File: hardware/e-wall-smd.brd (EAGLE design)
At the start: 50.8 x 48.3 mm, 66 parts, among them IC1 74HCT595D, IC2 74HCT595D, IC3 74HCT595D, IC4 74HCT595D, Q1 2N7002P, Q10 2N7002P, Q11 2N7002P, Q12 2N7002P, Q13 2N7002P, Q14 2N7002P, Q15 2N7002P, Q16 2N7002P, Q17 2N7002P, Q18 2N7002P, Q19 2N7002P, Q2 2N7002P, Q20 2N7002P, Q21 2N7002P, Q22 2N7002P, Q23 2N7002P, Q24 2N7002P, Q25 IRF8313P, Q26 IRF8313P, Q27 IRF8313P, Q28 IRF8313P, Q29 2N7002P, Q3 2N7002P, Q30 2N7002P, Q31 BSS84, Q4 2N7002P, Q5 2N7002P, Q6 2N7002P, Q7 2N7002P, Q8 2N7002P, Q9 2N7002P

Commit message: Transistortypen festgelegt
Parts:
- Q1, Q10, Q11, Q12, Q13, Q14, Q15, Q16, Q17, Q18, Q19, Q2, Q20, Q21, Q22, Q23, Q24, Q29, Q3, Q30, Q4, Q5, Q6, Q7, Q8, Q9: value 2N7002P -> SI2302CDS
- Q25, Q26, Q27, Q28: value IRF8313P -> SI4214DDY
- Q31: value BSS84 -> SI2347DS
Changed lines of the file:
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@@
 <element name="U$2" library="ultrasonic" package="HC-SR04" value="HC-SR04" x="25.4" y="2.54"/>
 <element name="U$1" library="msp430launchpad" package="MSP430LAUNCHPAD_BASIC" value="MSP430G2 Launchpad" x="25.4" y="13.97"/>
-<element name="Q1" library="transistor-small-signal" package="SOT23" value="2N7002P" x="8.89" y="26.67" rot="R90"/>
-<element name="Q2" library="transistor-small-signal" package="SOT23" value="2N7002P" x="8.89" y="27.94" rot="MR270"/>
-<element name="Q3" library="transistor-small-signal" package="SOT23" value="2N7002P" x="8.89" y="30.48" rot="R90"/>
-<element name="Q4" library="transistor-small-signal" package="SOT23" value="2N7002P" x="8.89" y="31.75" rot="MR270"/>
-<element name="Q5" library="transistor-small-signal" package="SOT23" value="2N7002P" x="8.89" y="35.56" rot="R90"/>
-<element name="Q6" library="transistor-small-signal" package="SOT23" value="2N7002P" x="8.89" y="36.83" rot="MR270"/>
-<element name="Q7" library="transistor-small-signal" package="SOT23" value="2N7002P" x="8.89" y="39.37" rot="R90"/>
-<element name="Q8" library="transistor-small-signal" package="SOT23" value="2N7002P" x="8.89" y="40.64" rot="MR270"/>
-<element name="Q9" library="transistor-small-signal" package="SOT23" value="2N7002P" x="31.75" y="39.37"/>
-<element name="Q10" library="transistor-small-signal" package="SOT23" value="2N7002P" x="30.48" y="39.37" rot="MR0"/>
-<element name="Q11" library="transistor-small-signal" package="SOT23" value="2N7002P" x="27.94" y="39.37"/>
-<element name="Q12" library="transistor-small-signal" package="SOT23" value="2N7002P" x="26.67" y="39.37" rot="MR0"/>
-<element name="Q13" library="transistor-small-signal" package="SOT23" value="2N7002P" x="24.13" y="39.37"/>
-<element name="Q14" library="transistor-small-signal" package="SOT23" value="2N7002P" x="22.86" y="39.37" rot="MR0"/>
-<element name="Q15" library="transistor-small-signal" package="SOT23" value="2N7002P" x="20.32" y="39.37"/>
-<element name="Q16" library="transistor-small-signal" package="SOT23" value="2N7002P" x="19.05" y="39.37" rot="MR0"/>
-<element name="Q17" library="transistor-small-signal" package="SOT23" value="2N7002P" x="41.91" y="40.64" rot="R270"/>
-<element name="Q18" library="transistor-small-signal" package="SOT23" value="2N7002P" x="41.91" y="39.37" rot="MR90"/>
-<element name="Q19" library="transistor-small-signal" package="SOT23" value="2N7002P" x="41.91" y="36.83" rot="R270"/>
-<element name="Q20" library="transistor-small-signal" package="SOT23" value="2N7002P" x="41.91" y="35.56" rot="MR90"/>
-<element name="Q21" library="transistor-small-signal" package="SOT23" value="2N7002P" x="41.91" y="33.02" rot="R270"/>
-<element name="Q22" library="transistor-small-signal" package="SOT23" value="2N7002P" x="41.91" y="31.75" rot="MR90"/>
-<element name="Q23" library="transistor-small-signal" package="SOT23" value="2N7002P" x="41.91" y="29.21" rot="R270"/>
-<element name="Q24" library="transistor-small-signal" package="SOT23" value="2N7002P" x="41.91" y="27.94" rot="MR90"/>
+<element name="Q1" library="transistor-small-signal" package="SOT23" value="SI2302CDS" x="8.89" y="26.67" rot="R90"/>
+<element name="Q2" library="transistor-small-signal" package="SOT23" value="SI2302CDS" x="8.89" y="27.94" rot="MR270"/>
+<element name="Q3" library="transistor-small-signal" package="SOT23" value="SI2302CDS" x="8.89" y="30.48" rot="R90"/>
+<element name="Q4" library="transistor-small-signal" package="SOT23" value="SI2302CDS" x="8.89" y="31.75" rot="MR270"/>
+<element name="Q5" library="transistor-small-signal" package="SOT23" value="SI2302CDS" x="8.89" y="35.56" rot="R90"/>
+<element name="Q6" library="transistor-small-signal" package="SOT23" value="SI2302CDS" x="8.89" y="36.83" rot="MR270"/>
+<element name="Q7" library="transistor-small-signal" package="SOT23" value="SI2302CDS" x="8.89" y="39.37" rot="R90"/>
+<element name="Q8" library="transistor-small-signal" package="SOT23" value="SI2302CDS" x="8.89" y="40.64" rot="MR270"/>
+<element name="Q9" library="transistor-small-signal" package="SOT23" value="SI2302CDS" x="31.75" y="39.37"/>
+<element name="Q10" library="transistor-small-signal" package="SOT23" value="SI2302CDS" x="30.48" y="39.37" rot="MR0"/>
+<element name="Q11" library="transistor-small-signal" package="SOT23" value="SI2302CDS" x="27.94" y="39.37"/>
+<element name="Q12" library="transistor-small-signal" package="SOT23" value="SI2302CDS" x="26.67" y="39.37" rot="MR0"/>
+<element name="Q13" library="transistor-small-signal" package="SOT23" value="SI2302CDS" x="24.13" y="39.37"/>
+<element name="Q14" library="transistor-small-signal" package="SOT23" value="SI2302CDS" x="22.86" y="39.37" rot="MR0"/>
+<element name="Q15" library="transistor-small-signal" package="SOT23" value="SI2302CDS" x="20.32" y="39.37"/>
+<element name="Q16" library="transistor-small-signal" package="SOT23" value="SI2302CDS" x="19.05" y="39.37" rot="MR0"/>
+<element name="Q17" library="transistor-small-signal" package="SOT23" value="SI2302CDS" x="41.91" y="40.64" rot="R270"/>
+<element name="Q18" library="transistor-small-signal" package="SOT23" value="SI2302CDS" x="41.91" y="39.37" rot="MR90"/>
+<element name="Q19" library="transistor-small-signal" package="SOT23" value="SI2302CDS" x="41.91" y="36.83" rot="R270"/>
+<element name="Q20" library="transistor-small-signal" package="SOT23" value="SI2302CDS" x="41.91" y="35.56" rot="MR90"/>
+<element name="Q21" library="transistor-small-signal" package="SOT23" value="SI2302CDS" x="41.91" y="33.02" rot="R270"/>
+<element name="Q22" library="transistor-small-signal" package="SOT23" value="SI2302CDS" x="41.91" y="31.75" rot="MR90"/>
+<element name="Q23" library="transistor-small-signal" package="SOT23" value="SI2302CDS" x="41.91" y="29.21" rot="R270"/>
+<element name="Q24" library="transistor-small-signal" package="SOT23" value="SI2302CDS" x="41.91" y="27.94" rot="MR90"/>
 <element name="D1" library="diode" package="SOT23" value="BAS40-05" x="3.81" y="29.21" rot="MR270"/>
 <element name="D2" library="diode" package="SOT23" value="BAS40-05" x="3.81" y="34.29" rot="MR270"/>
@@
 <element name="D12" library="diode" package="SOT23" value="BAS40-05" x="46.99" y="29.21" rot="MR90"/>
 <element name="IC4" library="74xx-eu" package="SO16" value="74HCT595D" x="25.4" y="15.24"/>
-<element name="Q25" library="transistor-power" package="SO-08" value="IRF8313P" x="19.05" y="16.51" rot="MR270"/>
-<element name="Q26" library="transistor-power" package="SO-08" value="IRF8313P" x="19.05" y="10.16" rot="MR270"/>
-<element name="Q27" library="transistor-power" package="SO-08" value="IRF8313P" x="31.75" y="10.16" rot="MR90"/>
-<element name="Q28" library="transistor-power" package="SO-08" value="IRF8313P" x="31.75" y="16.51" rot="MR90"/>
+<element name="Q25" library="transistor-power" package="SO-08" value="SI4214DDY" x="19.05" y="16.51" rot="MR270"/>
+<element name="Q26" library="transistor-power" package="SO-08" value="SI4214DDY" x="19.05" y="10.16" rot="MR270"/>
+<element name="Q27" library="transistor-power" package="SO-08" value="SI4214DDY" x="31.75" y="10.16" rot="MR90"/>
+<element name="Q28" library="transistor-power" package="SO-08" value="SI4214DDY" x="31.75" y="16.51" rot="MR90"/>
 <element name="SV4" library="con-lstb" package="MA04-2" value="" x="11.43" y="15.24" rot="MR90">
 <attribute name="OC_NEWARK" value="unknown" x="11.43" y="15.24" size="1.778" layer="28" rot="MR90" display="off"/>
@@
 <attribute name="TP_SIGNAL_NAME" value="" x="35.56" y="39.37" size="1.778" layer="27" display="off"/>
 </element>
-<element name="Q29" library="transistor-small-signal" package="SOT23" value="2N7002P" x="38.1" y="2.54" rot="MR90"/>
-<element name="Q30" library="transistor-small-signal" package="SOT23" value="2N7002P" x="12.7" y="3.81" rot="R270"/>
-<element name="Q31" library="transistor-small-signal" package="SOT23" value="BSS84" x="22.86" y="5.08" rot="R270"/>
+<element name="Q29" library="transistor-small-signal" package="SOT23" value="SI2302CDS" x="38.1" y="2.54" rot="MR90"/>
+<element name="Q30" library="transistor-small-signal" package="SOT23" value="SI2302CDS" x="12.7" y="3.81" rot="R270"/>
+<element name="Q31" library="transistor-small-signal" package="SOT23" value="SI2347DS" x="22.86" y="5.08" rot="R270"/>
 </elements>
 <signals>

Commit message: kleine Anpassungen im Schema, erc bereinigt
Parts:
- SV1, SV2, SV3: value (none) -> 8x2
- SV4, SV5: value (none) -> 4x2
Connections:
- net +5V: now also U$2.1; no longer U$2.P$1
- net ECHO: now also U$2.3; no longer U$2.P$3
- net GND: now also U$2.4; no longer U$2.P$4
- net TRIGGER: now also U$2.2; no longer U$2.P$2
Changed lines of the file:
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@@
 <element name="R6" library="resistor" package="R1206" value="4.7k" x="27.94" y="5.08" rot="R180"/>
 <element name="R7" library="resistor" package="R1206" value="100k" x="6.35" y="3.81" rot="MR0"/>
-<element name="SV1" library="con-lsta" package="FE08-2" value="" x="3.81" y="36.83" rot="MR270">
+<element name="SV1" library="con-lsta" package="FE08-2" value="8x2" x="3.81" y="36.83" rot="MR270">
 <attribute name="OC_NEWARK" value="unknown" x="66.04" y="-12.7" size="1.778" layer="28" rot="MR270" display="off"/>
 <attribute name="MPN" value="" x="66.04" y="-12.7" size="1.778" layer="28" rot="MR270" display="off"/>
@@
 <attribute name="OC_FARNELL" value="unknown" x="66.04" y="-12.7" size="1.778" layer="28" rot="MR270" display="off"/>
 </element>
-<element name="SV2" library="con-lsta" package="FE08-2" value="" x="25.4" y="44.45">
+<element name="SV2" library="con-lsta" package="FE08-2" value="8x2" x="25.4" y="44.45">
 <attribute name="OC_NEWARK" value="unknown" x="96.52" y="-17.78" size="1.778" layer="27" display="off"/>
 <attribute name="MPN" value="" x="96.52" y="-17.78" size="1.778" layer="27" display="off"/>
@@
 <attribute name="OC_FARNELL" value="unknown" x="96.52" y="-17.78" size="1.778" layer="27" display="off"/>
 </element>
-<element name="SV3" library="con-lsta" package="FE08-2" value="" x="46.99" y="36.83" rot="MR90">
+<element name="SV3" library="con-lsta" package="FE08-2" value="8x2" x="46.99" y="36.83" rot="MR90">
 <attribute name="OC_NEWARK" value="unknown" x="-27.94" y="60.96" size="1.778" layer="28" rot="MR90" display="off"/>
 <attribute name="MPN" value="" x="-27.94" y="60.96" size="1.778" layer="28" rot="MR90" display="off"/>
@@
 <element name="Q27" library="transistor-power" package="SO-08" value="SI4214DDY" x="31.75" y="10.16" rot="MR90"/>
 <element name="Q28" library="transistor-power" package="SO-08" value="SI4214DDY" x="31.75" y="16.51" rot="MR90"/>
-<element name="SV4" library="con-lstb" package="MA04-2" value="" x="11.43" y="15.24" rot="MR90">
+<element name="SV4" library="con-lstb" package="MA04-2" value="4x2" x="11.43" y="15.24" rot="MR90">
 <attribute name="OC_NEWARK" value="unknown" x="11.43" y="15.24" size="1.778" layer="28" rot="MR90" display="off"/>
 <attribute name="MPN" value="" x="11.43" y="15.24" size="1.778" layer="28" rot="MR90" display="off"/>
@@
 <attribute name="OC_FARNELL" value="unknown" x="11.43" y="15.24" size="1.778" layer="28" rot="MR90" display="off"/>
 </element>
-<element name="SV5" library="con-lstb" package="MA04-2" value="" x="39.37" y="15.24" rot="MR270">
+<element name="SV5" library="con-lstb" package="MA04-2" value="4x2" x="39.37" y="15.24" rot="MR270">
 <attribute name="OC_NEWARK" value="unknown" x="39.37" y="15.24" size="1.778" layer="28" rot="MR270" display="off"/>
 <attribute name="MPN" value="" x="39.37" y="15.24" size="1.778" layer="28" rot="MR270" display="off"/>
@@
 <signal name="ECHO">
 <contactref element="R1" pad="2"/>
-<contactref element="U$2" pad="P$3"/>
+<contactref element="U$2" pad="3"/>
 <wire x1="7.772" y1="2.54" x2="8.636" y2="2.54" width="0.4064" layer="1"/>
 <wire x1="8.636" y1="2.54" x2="10.16" y2="1.016" width="0.4064" layer="1"/>
@@
 <signal name="TRIGGER">
 <contactref element="R6" pad="2"/>
-<contactref element="U$2" pad="P$2"/>
+<contactref element="U$2" pad="2"/>
 <contactref element="Q31" pad="3"/>
 <wire x1="24.13" y1="2.54" x2="24.13" y2="4.91" width="0.4064" layer="1"/>
@@
 <signal name="+5V" class="1">
 <contactref element="R4" pad="2"/>
-<contactref element="U$2" pad="P$1"/>
+<contactref element="U$2" pad="1"/>
 <contactref element="IC1" pad="10"/>
 <contactref element="IC2" pad="10"/>
@@
 <contactref element="R6" pad="1"/>
 <contactref element="R9" pad="1"/>
-<contactref element="U$2" pad="P$4"/>
+<contactref element="U$2" pad="4"/>
 <contactref element="U$1" pad="20"/>
 <contactref element="Q6" pad="2"/>

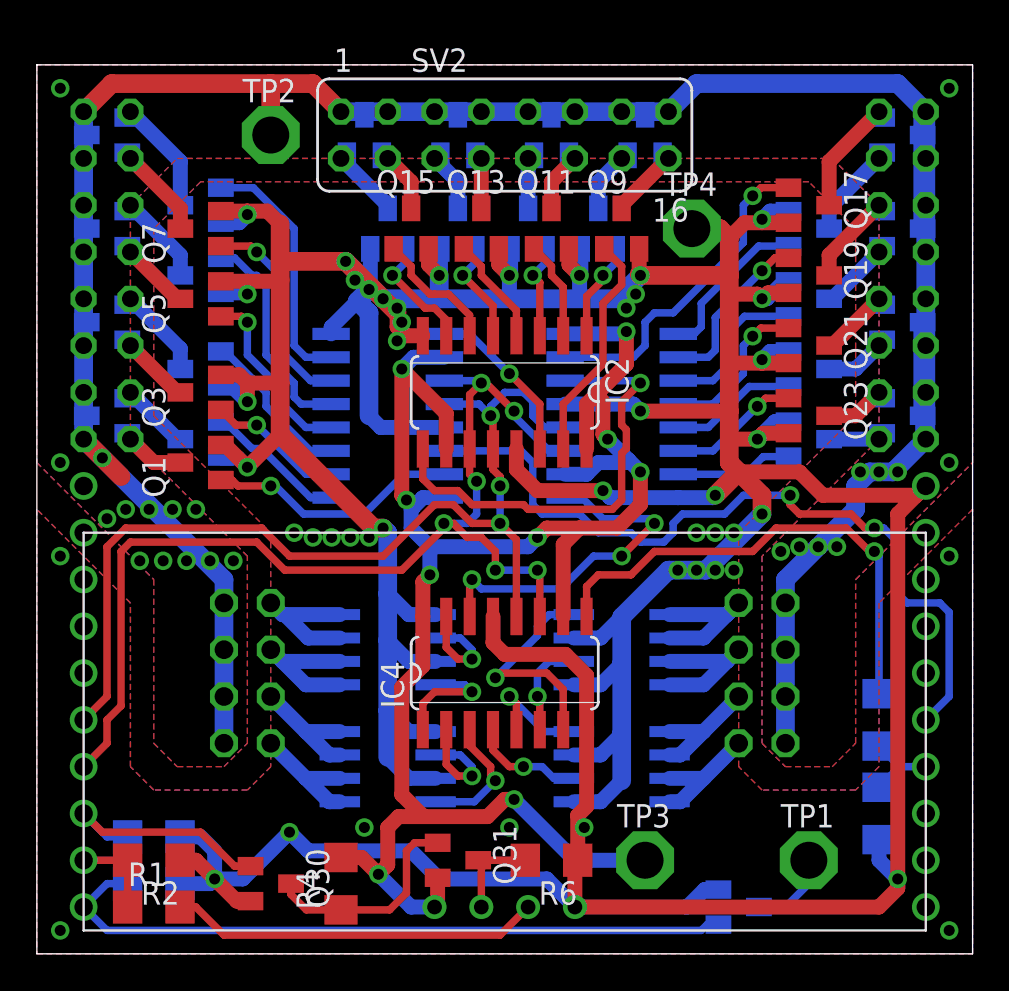
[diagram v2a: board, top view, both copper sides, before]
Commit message: Kondensatoren ergänzt
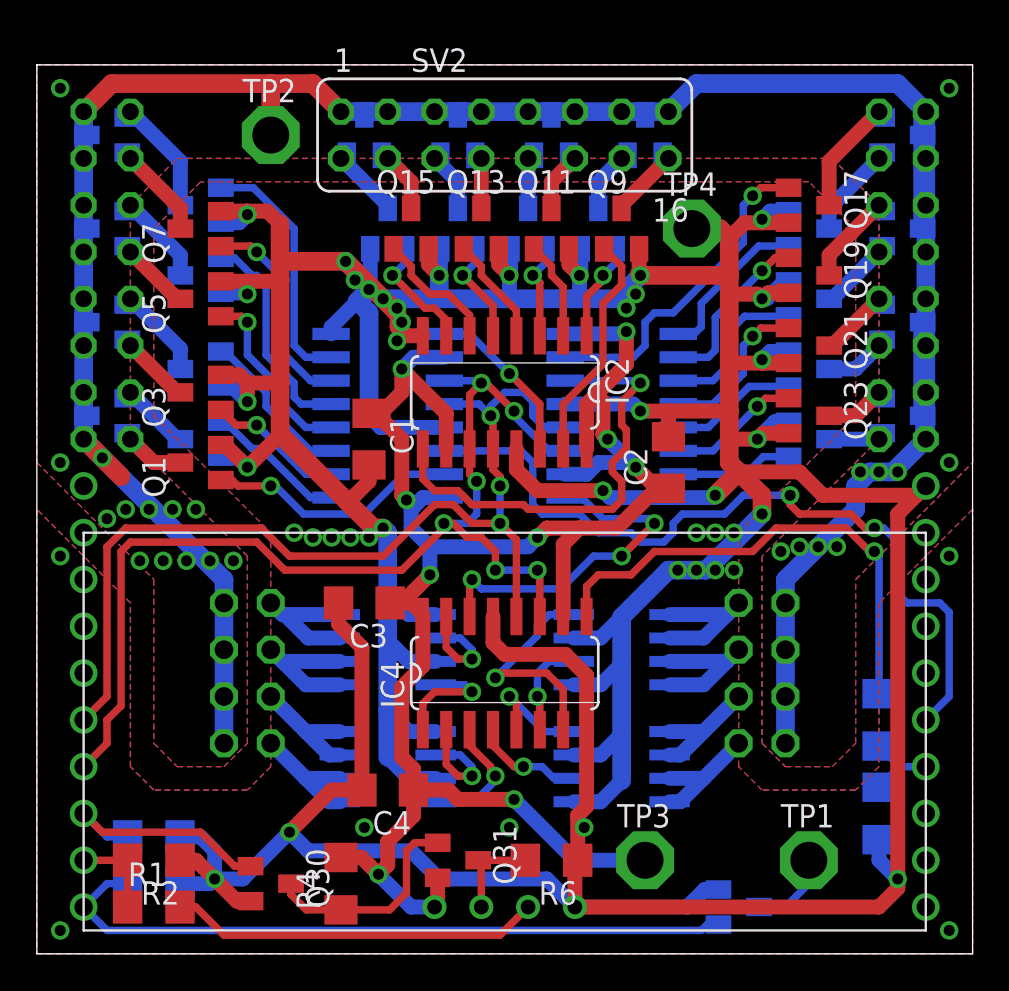
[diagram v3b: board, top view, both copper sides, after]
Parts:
- added C1, C2, C3, C4: 33n, resistor:C1206
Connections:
- net +5V: now also C1.1, C2.1, C3.1, C4.1
- net GND: now also C1.2, C2.2, C3.2, C4.2
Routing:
- net GND: track 339.2 -> 358.7 mm
- net +5V: track 101.5 -> 105.9 mm
